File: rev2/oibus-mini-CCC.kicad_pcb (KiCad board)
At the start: 2 copper layers, 37 x 60 mm, 90 parts, among them J1 Conn_01x04_Female, J2 USB_B_Micro, J3 uavcan_5pins, J4 Conn_01x02_Female, P1 TC2030-MCP, Q1 DMG3415U-7, Q2 NMOS, Q3 NMOS, SW1 SW_Push, U1 AP2112K-3.3, U10 TPD3E001DRLR, U2 SAM-M8Q, U3 NINA-B311-00B, U4 MCP73831-2-OT, U5 MCP1624T, U6 SHT31-DIS-B, U7 TCAN330, U8 STM32F303CCTx, U9 DW01C-G, Y1 16M, Y2 32kHz

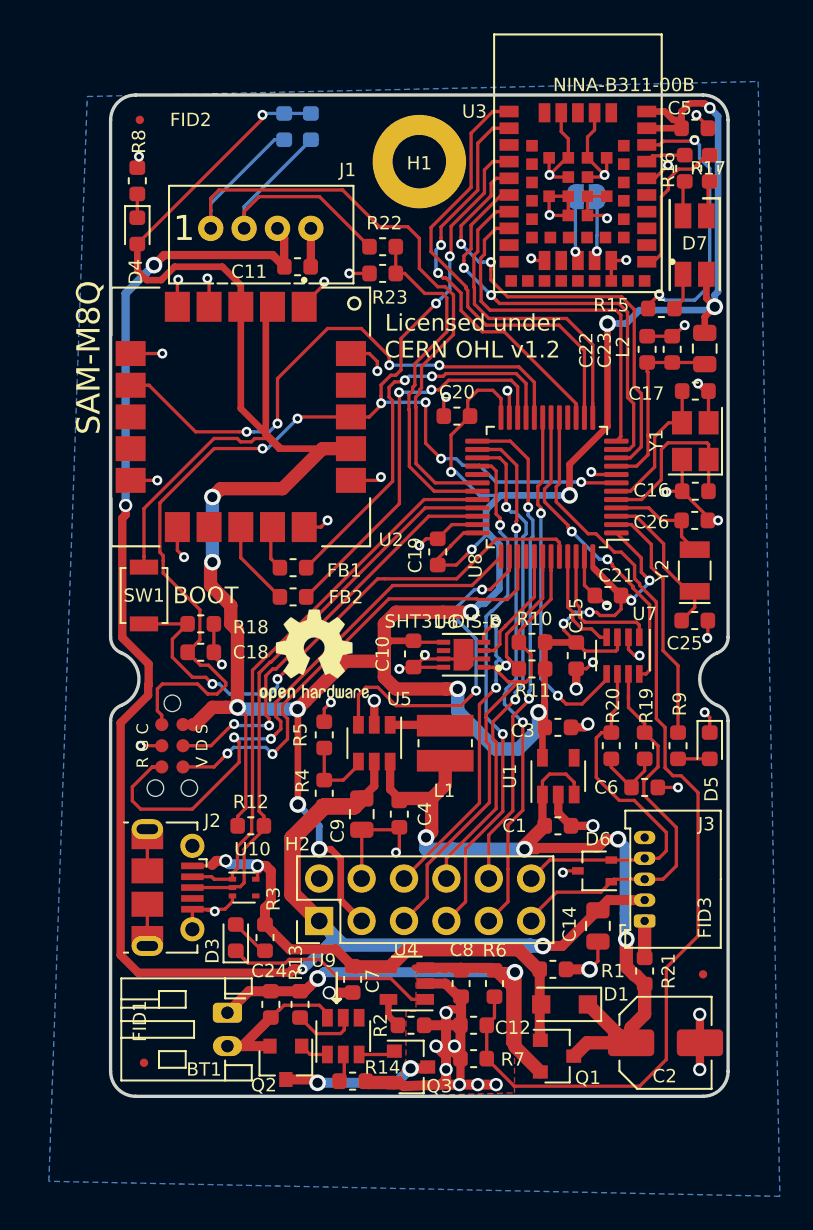
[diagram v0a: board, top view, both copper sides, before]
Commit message: added cut-out for SHT sensor, rotated battery connector, added on-off button
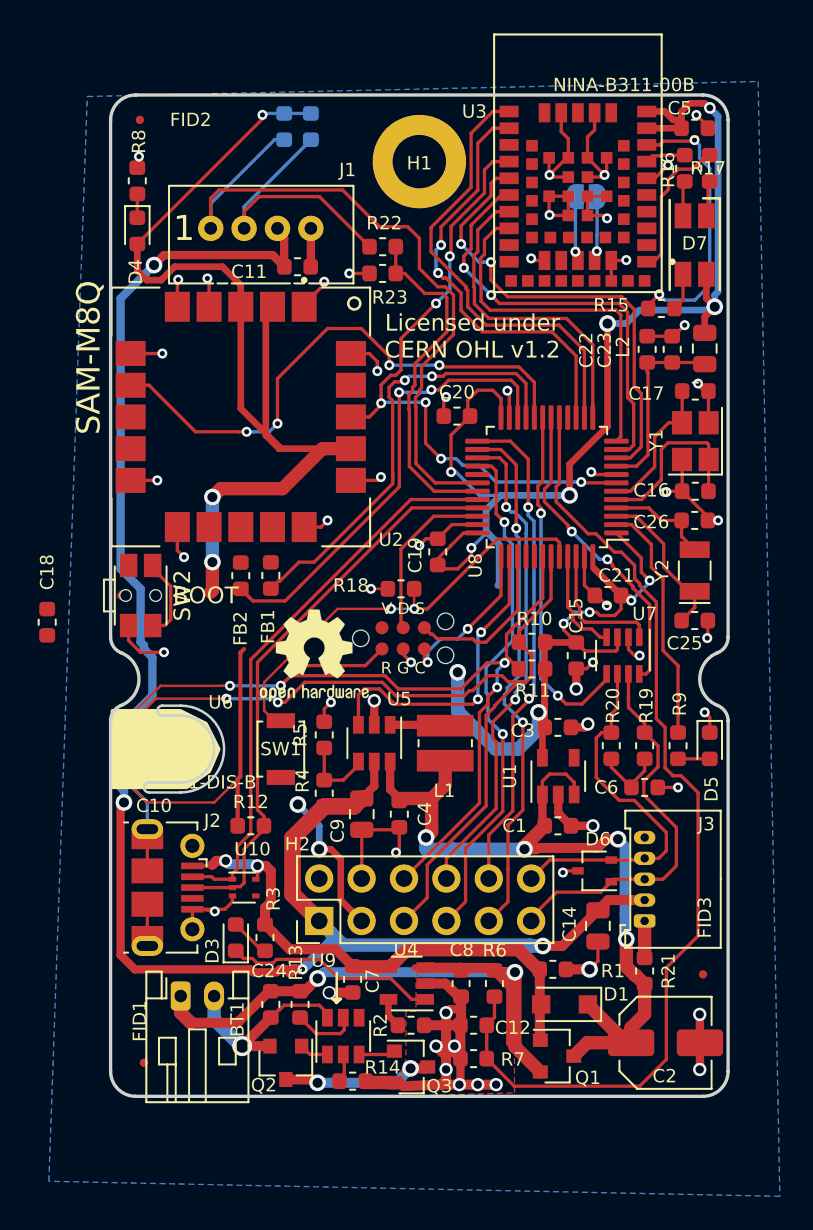
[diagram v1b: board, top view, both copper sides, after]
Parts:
- added SW2: SW_Push, Button_Switch_SMD:SW_SPST_EVQP7C, F.Cu at (1.80, -30.0)
- moved C10 18.1 mm to (1.20, -20.2), turned to 270 degrees
- moved U6 18.1 mm to (4.00, -20.8), turned to 0 degrees
- moved P1 15.3 mm to (17.5, -27.4), turned to 0 degrees
- moved SW1 12.3 mm to (10.2, -20.8), turned to 270 degrees
- moved R18 12.2 mm to (17.4, -30.4), turned to 180 degrees
- moved C18 9.37 mm to (-3.80, -28.4), turned to 90 degrees
- moved FB2 3.38 mm to (7.80, -31.2), turned to 90 degrees
- moved BT1 2.97 mm to (4.20, -6.00), turned to 0 degrees
- moved FB1 1.41 mm to (9.60, -31.2), turned to 90 degrees
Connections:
- U6 pad 3: /SHT_ALERT -> (no net)
- U8 pad 29: (no net) -> /on_off
- U8 pad 41: /SHT_ALERT -> (no net)
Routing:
- net +3V3: track 246.3 -> 203.7 mm, vias 20 -> 17
- net /~RESET: track 71.9 -> 43.4 mm, vias 8 -> 6
- net /SCL: track 28.4 -> 53.4 mm, vias 3 -> 4
- net /SWDCLK: track 34.5 -> 9.64 mm
- net /SDA: track 29.3 -> 53.3 mm, vias 0 -> 2
- net /SWDSWO: track 28.3 -> 9.97 mm, vias 2 -> 0
- net /SWDIO: track 25.5 -> 10.2 mm, vias 2 -> 0
- net /BOOT: track 34.3 -> 26.3 mm
- net /SHT_ALERT: track 7.25 -> 0.00 mm
- net GND: track 147.7 -> 154.5 mm
- net Net-(FB2-Pad2): track 5.15 -> 0.00 mm
- net /on_off: track 0.00 -> 4.92 mm
- net +BATT: track 39.2 -> 43.5 mm
- net GPS_TX: track 24.0 -> 27.9 mm
- net GPS_RX: track 23.9 -> 27.2 mm
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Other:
- outline, holes or cut-outs redrawn

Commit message: finished all layout changes for REV2. todo: silkscreen labels
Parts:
- moved C18 10.6 mm to (6.80, -27.8), turned to 180 degrees
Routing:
- net +3V3: track 203.7 -> 252.3 mm, vias 17 -> 19
- net /on_off: track 4.92 -> 28.8 mm, vias 0 -> 2
- net /~RESET: track 43.4 -> 65.4 mm, vias 6 -> 9
- net GND: track 154.5 -> 161.8 mm, vias 56 -> 58
- net Net-(FB1-Pad2): track 0.00 -> 2.15 mm
- net Net-(FB2-Pad2): track 0.00 -> 2.12 mm
- net SPS_RX: track 42.9 -> 41.6 mm
- net /BOOT: track 26.3 -> 27.4 mm, vias 2 -> 0
- net /SDA: track 53.3 -> 52.8 mm
- net /SWDIO: vias 0 -> 2
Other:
- rule trace_min: 0.2 -> 0.15
- board text added: "Air Quality Sensor Board"
- board text added: "Made with KiCad by octanis.ch"
- board text added: "Rev 2, 11.2019, RT For research purposes only, not approved for resale."
- board text added: "climatecitycup.org"
- board text removed: "Air Quality Sensor Board Made with KiCad by Octanis Instruments www.octanis.ch"
- board text removed: "Rev 1, 10.2019, RT For research purposes only, not approved for resale."

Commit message: finished silkscreen V2, generated GERBER files
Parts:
- moved REF** 1.03 mm to (11.7, -27.3)
- renumbered J4 to NFC
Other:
- board text added: "BAT-"
- board text added: "BLUETOOTH"
- board text added: "CHG/ PROG"
- board text added: "Li-Ion Battery 3 - 4.2 V"
- board text added: "PWR"
- board text added: "UAVCAN"
- board text removed: "CAN"
- board text removed: "GPS"
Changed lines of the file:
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@@
   (general
     (thickness 1.6)
-    (drawings 52)
+    (drawings 56)
     (tracks 1427)
     (zones 0)
@@
   (page A4)
   (layers
-    (0 F.Cu signal)
-    (31 B.Cu signal)
+    (0 F.Cu signal hide)
+    (31 B.Cu signal hide)
     (32 B.Adhes user hide)
     (33 F.Adhes user hide)
     (35 F.Paste user hide)
     (36 B.SilkS user hide)
-    (37 F.SilkS user hide)
+    (37 F.SilkS user)
     (38 B.Mask user)
-    (39 F.Mask user hide)
+    (39 F.Mask user)
     (40 Dwgs.User user)
     (41 Cmts.User user)
@@
       (plotinvisibletext false)
       (padsonsilk false)
-      (subtractmaskfromsilk false)
+      (subtractmaskfromsilk true)
       (outputformat 1)
       (mirror false)
@@
     (tags capacitor)
     (attr smd)
-    (fp_text reference C18 (at 3 0 180) (layer F.SilkS)
+    (fp_text reference C18 (at 0.15 1.3 180) (layer F.SilkS)
       (effects (font (size 0.8 0.8) (thickness 0.15)))
     )
@@
     (tags capacitor)
     (attr smd)
-    (fp_text reference C19 (at 0.2 1.35 270) (layer F.SilkS)
+    (fp_text reference C19 (at -2.7375 0.05 270) (layer F.SilkS)
       (effects (font (size 0.8 0.8) (thickness 0.15)))
     )
@@
     (tags capacitor)
     (attr smd)
-    (fp_text reference C14 (at 0.1 -1.7 -90) (layer F.SilkS)
+    (fp_text reference C14 (at 0.25 -1.45 -90) (layer F.SilkS)
       (effects (font (size 0.8 0.8) (thickness 0.15)))
     )
@@
     (tags fiducial)
     (attr smd)
-    (fp_text reference FID1 (at -0.25 -2.5 90) (layer F.SilkS)
+    (fp_text reference FID1 (at -0.8 -1.85 90) (layer F.SilkS)
       (effects (font (size 0.8 0.8) (thickness 0.15)))
     )
@@
     (tags diode)
     (attr smd)
-    (fp_text reference D4 (at 2.45 0.1 90) (layer F.SilkS)
+    (fp_text reference D4 (at 2.3 0.05 90) (layer F.SilkS)
       (effects (font (size 0.8 0.8) (thickness 0.15)))
     )
@@
     (at 4 -20.8)
     (attr smd)
-    (fp_text reference U6 (at 2.6 -2.8) (layer F.SilkS)
+    (fp_text reference U6 (at -0.05 -3.55) (layer F.SilkS)
       (effects (font (size 0.8 0.8) (thickness 0.15)))
     )
@@
     (tags capacitor)
     (attr smd)
-    (fp_text reference C10 (at 2.8 -1.4) (layer F.SilkS)
+    (fp_text reference C10 (at 2.65 -1.2) (layer F.SilkS)
       (effects (font (size 0.8 0.8) (thickness 0.15)))
     )
@@
     (tags inductor)
     (attr smd)
-    (fp_text reference FB1 (at -3.066631 -0.167542 90) (layer F.SilkS)
+    (fp_text reference FB1 (at 0.3 2.8 90) (layer F.SilkS)
       (effects (font (size 0.8 0.8) (thickness 0.15)))
     )
@@
     (tags inductor)
     (attr smd)
-    (fp_text reference FB2 (at -3.166631 -0.017542 90) (layer F.SilkS)
+    (fp_text reference FB2 (at 0.2625 3.4 90) (layer F.SilkS)
       (effects (font (size 0.8 0.8) (thickness 0.15)))
     )
@@
     (descr "JST PH series connector, S2B-PH-K (http://www.jst-mfg.com/product/pdf/eng/ePH.pdf), generated with kicad-footprint-generator")
     (tags "connector JST PH top entry")
-    (fp_text reference BT1 (at 3.4 1.4 -90) (layer F.SilkS)
+    (fp_text reference BT1 (at 1.15 1.5 180) (layer F.SilkS)
       (effects (font (size 0.8 0.8) (thickness 0.15)))
     )
@@
     (tags capacitor)
     (attr smd)
-    (fp_text reference C9 (at -1 -1.45 90) (layer F.SilkS)
+    (fp_text reference C9 (at -1.1 -1.45 90) (layer F.SilkS)
       (effects (font (size 0.8 0.8) (thickness 0.15)))
     )
@@
     (tags resistor)
     (attr smd)
-    (fp_text reference R4 (at 0.75 -1.3 90) (layer F.SilkS)
+    (fp_text reference R4 (at -2.25 -0.25 90) (layer F.SilkS)
       (effects (font (size 0.8 0.8) (thickness 0.15)))
     )
@@
     (tags resistor)
     (attr smd)
-    (fp_text reference R5 (at 0 -1.43 90) (layer F.SilkS)
+    (fp_text reference R5 (at 2.25 -0.35 90) (layer F.SilkS)
       (effects (font (size 0.8 0.8) (thickness 0.15)))
     )
@@
     (tags resistor)
     (attr smd)
-    (fp_text reference R6 (at -1.99 -0.02) (layer F.SilkS)
+    (fp_text reference R6 (at -1.85 -0.02) (layer F.SilkS)
       (effects (font (size 0.8 0.8) (thickness 0.15)))
     )
@@
     (tags SOT-23-5)
     (attr smd)
-    (fp_text reference U4 (at 0.05 2.05 180) (layer F.SilkS)
+    (fp_text reference U4 (at 0 1.95 180) (layer F.SilkS)
       (effects (font (size 0.8 0.8) (thickness 0.15)))
     )
@@
     (tags resistor)
     (attr smd)
-    (fp_text reference R1 (at 3.6 0.1) (layer F.SilkS)
+    (fp_text reference R1 (at 0.8 -1.05) (layer F.SilkS)
       (effects (font (size 0.8 0.8) (thickness 0.15)))
     )
@@
     (tags resistor)
     (attr smd)
-    (fp_text reference R16 (at 0.1 1 90) (layer F.SilkS)
-      (effects (font (size 0.8 0.8) (thickness 0.15)))
+    (fp_text reference R16 (at -1.6 0.5 180) (layer F.SilkS)
+      (effects (font (size 0.6 0.6) (thickness 0.15)))
     )
     (fp_text value 1k (at 0 1.43 270) (layer F.Fab)
@@
     (tags resistor)
     (attr smd)
-    (fp_text reference R17 (at 0 0.1 180) (layer F.SilkS)
-      (effects (font (size 0.8 0.8) (thickness 0.15)))
+    (fp_text reference R17 (at -1.55 -0.1 180) (layer F.SilkS)
+      (effects (font (size 0.6 0.6) (thickness 0.15)))
     )
     (fp_text value 2k7 (at 0 1.43 270) (layer F.Fab)
@@
     (tags resistor)
     (attr smd)
-    (fp_text reference R18 (at 3 0.2 180) (layer F.SilkS)
+    (fp_text reference R18 (at 3.25 0 180) (layer F.SilkS)
       (effects (font (size 0.8 0.8) (thickness 0.15)))
     )
@@
     (tags "solder jumper open")
     (attr virtual)
-    (fp_text reference J4 (at 0 1.8 180) (layer B.SilkS)
+    (fp_text reference NFC (at 0 1.8 180) (layer B.SilkS)
       (effects (font (size 0.8 0.8) (thickness 0.15)) (justify mirror))
     )
@@
   )
   (module Symbol:OSHW-Logo2_7.3x6mm_SilkScreen (layer F.Cu)
-    (at 12.2 -26.4)
+    (at 11.7 -27.3)
     (descr "Open Source Hardware Symbol")
     (tags "Logo Symbol OSHW")
@@
     (tags capacitor)
     (attr smd)
-    (fp_text reference C8 (at 2.02 0.04 180) (layer F.SilkS)
+    (fp_text reference C8 (at 1.85 0.04 180) (layer F.SilkS)
       (effects (font (size 0.8 0.8) (thickness 0.15)))
     )
@@
     (descr "Light Touch Switch")
     (attr smd)
-    (fp_text reference SW2 (at 0 -2.5 270) (layer F.SilkS)
-      (effects (font (size 1 1) (thickness 0.15)))
+    (fp_text reference SW2 (at 0 -0.1 270) (layer F.SilkS)
+      (effects (font (size 0.8 0.8) (thickness 0.15)))
     )
     (fp_text value SW_Push (at 0 3.25 270) (layer F.Fab)
@@
     )
   )
+  (gr_poly (pts (xy 0 -23) (xy 4.4 -23) (xy 5.8 -22.6) (xy 6.4 -21.2) (xy 6.4 -20.2) (xy 5.8 -19.2) (xy 4.6 -18.4) (xy 2.4 -18.4) (xy 0 -18.4)) (layer F.SilkS) (width 0.15))
+  (gr_text PWR (at 4.55 -30 270) (layer F.SilkS)
+    (effects (font (size 1 1) (thickness 0.2)))
+  )
+  (gr_text "CHG/\nPROG" (at 2.25 -12.6 270) (layer B.SilkS)
+    (effects (font (size 1 1) (thickness 0.2)) (justify mirror))
+  )
+  (gr_text "UAVCAN\n" (at 34.7 -12.95 90) (layer B.SilkS)
+    (effects (font (size 1 1) (thickness 0.2)) (justify mirror))
+  )
+  (gr_text "Li-Ion Battery\n3 - 4.2 V" (at 11.9 -4.2) (layer B.SilkS)
+    (effects (font (size 0.8 0.8) (thickness 0.2)) (justify mirror))
+  )
   (gr_text climatecitycup.org (at 18.4 -33.8) (layer B.SilkS)
     (effects (font (size 1 1) (thickness 0.2)) (justify mirror))
@@
     (effects (font (size 1 1) (thickness 0.2)) (justify mirror))
   )
-  (gr_text BOOT (at 5.7 -30) (layer F.SilkS)
+  (gr_text BOOT (at 8 -20.7 270) (layer F.SilkS)
     (effects (font (size 1 1) (thickness 0.2)))
   )
@@
     (effects (font (size 1 1) (thickness 0.2)) (justify mirror))
   )
-  (gr_text GPS (at 35.9 -51 90) (layer B.SilkS)
+  (gr_text "BLUETOOTH\n" (at 36 -52.2 90) (layer B.SilkS)
     (effects (font (size 1 1) (thickness 0.2)) (justify mirror))
   )
-  (gr_text GND (at 6.2 -3 90) (layer B.SilkS)
+  (gr_text BAT- (at 6.25 -2.65 270) (layer B.SilkS)
     (effects (font (size 1.2 1.2) (thickness 0.25)) (justify mirror))
   )
-  (gr_text BAT+ (at 4.2 -2.6 90) (layer B.SilkS)
+  (gr_text BAT+ (at 4.2 -2.6 270) (layer B.SilkS)
     (effects (font (size 1.2 1.2) (thickness 0.25)) (justify mirror))
   )
@@
   (gr_arc (start 48.5 93.5) (end 48.5 96.25) (angle -180) (layer F.Fab) (width 0.15))
   (gr_arc (start 85.5 93.5) (end 85.5 90.75) (angle -180) (layer F.Fab) (width 0.15))
-  (gr_text "CAN\n" (at 35.9 -21.1 90) (layer B.SilkS)
-    (effects (font (size 1 1) (thickness 0.2)) (justify mirror))
-  )
   (gr_text "Rev 2, 11.2019, RT\nFor research purposes only,\nnot approved for resale." (at 36.4 -2.5) (layer B.SilkS)
     (effects (font (size 0.8 0.75) (thickness 0.15)) (justify left mirror))
@@
       )
     )
-  )
-  (zone (net 0) (net_name "") (layer F.SilkS) (hatch edge 0.508)
-    (connect_pads (clearance 0.3))
-    (min_thickness 0.254)
-    (fill yes (arc_segments 16) (thermal_gap 0.508) (thermal_bridge_width 0.508))
-    (polygon
-      (pts
-        (xy 0 -23.2) (xy 4.2 -23.2) (xy 5.8 -22.4) (xy 6.6 -20.8) (xy 6 -19.4)
-        (xy 4.6 -18.4) (xy 0 -18.4)
-      )
-    )
